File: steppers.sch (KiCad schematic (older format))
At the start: 24 parts, among them J1 HEADER, J10 STEPSTICK, J11 STEPSTICK, J12 STEPSTICK, J2 HEADER, J3 HEADER, J4 STEPSTICK, J5 STEPSTICK, J6 STEPSTICK, J7 HEADER, J8 HEADER, J9 HEADER, P10 CONN_01X04, P11 CONN_01X04, P12 CONN_01X04, P7 CONN_02X04, P8 CONN_01X04, P9 CONN_01X04

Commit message: Added component specifications
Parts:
- C12, C13, C14, C15, C16, C17: Manufacturer (none) -> United Chemi-Con; ManufacturerNo (none) -> EMZR500ADA101MF80G; VoltageRating (none) -> 50V
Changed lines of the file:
@@
 F 2 "capacitors:c_elec_6.3x7.7" H 3800 1425 50  0001 C CNN
 F 3 "" H 3800 1425 50  0000 C CNN
+F 4 "50V" H 3800 1425 135 0001 L CNN "VoltageRating"
+F 5 "EMZR500ADA101MF80G" H 3800 1425 135 0001 L CNN "ManufacturerNo"
+F 6 "United Chemi-Con" H 3800 1425 135 0001 L CNN "Manufacturer"
 	1    3800 1425
 	1    0    0    -1
@@
 F 2 "capacitors:c_elec_6.3x7.7" H 3800 2650 50  0001 C CNN
 F 3 "" H 3800 2650 50  0000 C CNN
+F 4 "50V" H 3800 2650 135 0001 L CNN "VoltageRating"
+F 5 "EMZR500ADA101MF80G" H 3800 2650 135 0001 L CNN "ManufacturerNo"
+F 6 "United Chemi-Con" H 3800 2650 135 0001 L CNN "Manufacturer"
 	1    3800 2650
 	1    0    0    -1
@@
 F 2 "capacitors:c_elec_6.3x7.7" H 3950 3950 50  0001 C CNN
 F 3 "" H 3950 3950 50  0000 C CNN
+F 4 "50V" H 3950 3950 135 0001 L CNN "VoltageRating"
+F 5 "United Chemi-Con" H 3950 3950 135 0001 L CNN "Manufacturer"
+F 6 "EMZR500ADA101MF80G" H 3950 3950 135 0001 L CNN "ManufacturerNo"
 	1    3950 3950
 	1    0    0    -1
@@
 F 2 "capacitors:c_elec_6.3x7.7" H 8900 4075 50  0001 C CNN
 F 3 "" H 8900 4075 50  0000 C CNN
+F 4 "50V" H 8900 4075 135 0001 L CNN "VoltageRating"
+F 5 "EMZR500ADA101MF80G" H 8900 4075 135 0001 L CNN "ManufacturerNo"
+F 6 "United Chemi-Con" H 8900 4075 135 0001 L CNN "Manufacturer"
 	1    8900 4075
 	1    0    0    -1
@@
 F 2 "capacitors:c_elec_6.3x7.7" H 8875 1400 50  0001 C CNN
 F 3 "" H 8875 1400 50  0000 C CNN
+F 4 "50V" H 8875 1400 135 0001 L CNN "VoltageRating"
+F 5 "EMZR500ADA101MF80G" H 8875 1400 135 0001 L CNN "ManufacturerNo"
+F 6 "United Chemi-Con" H 8875 1400 135 0001 L CNN "Manufacturer"
 	1    8875 1400
 	1    0    0    -1
@@
 F 2 "capacitors:c_elec_6.3x7.7" H 8875 2775 50  0001 C CNN
 F 3 "" H 8875 2775 50  0000 C CNN
+F 4 "50V" H 8875 2775 135 0001 L CNN "VoltageRating"
+F 5 "EMZR500ADA101MF80G" H 8875 2775 135 0001 L CNN "ManufacturerNo"
+F 6 "United Chemi-Con" H 8875 2775 135 0001 L CNN "Manufacturer"
 	1    8875 2775
 	1    0    0    -1

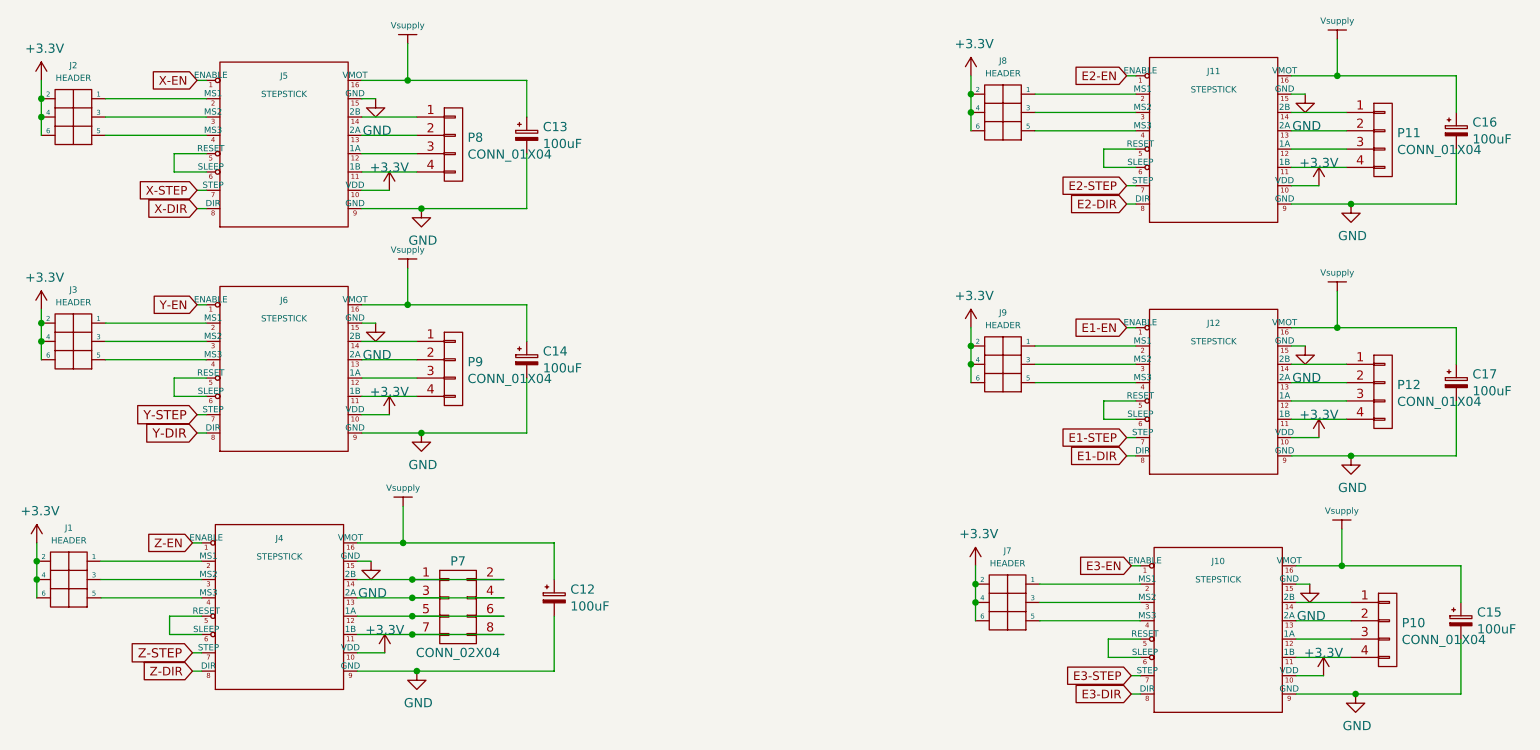
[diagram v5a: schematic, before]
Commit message: Added specifications and manufacturers to component attributes
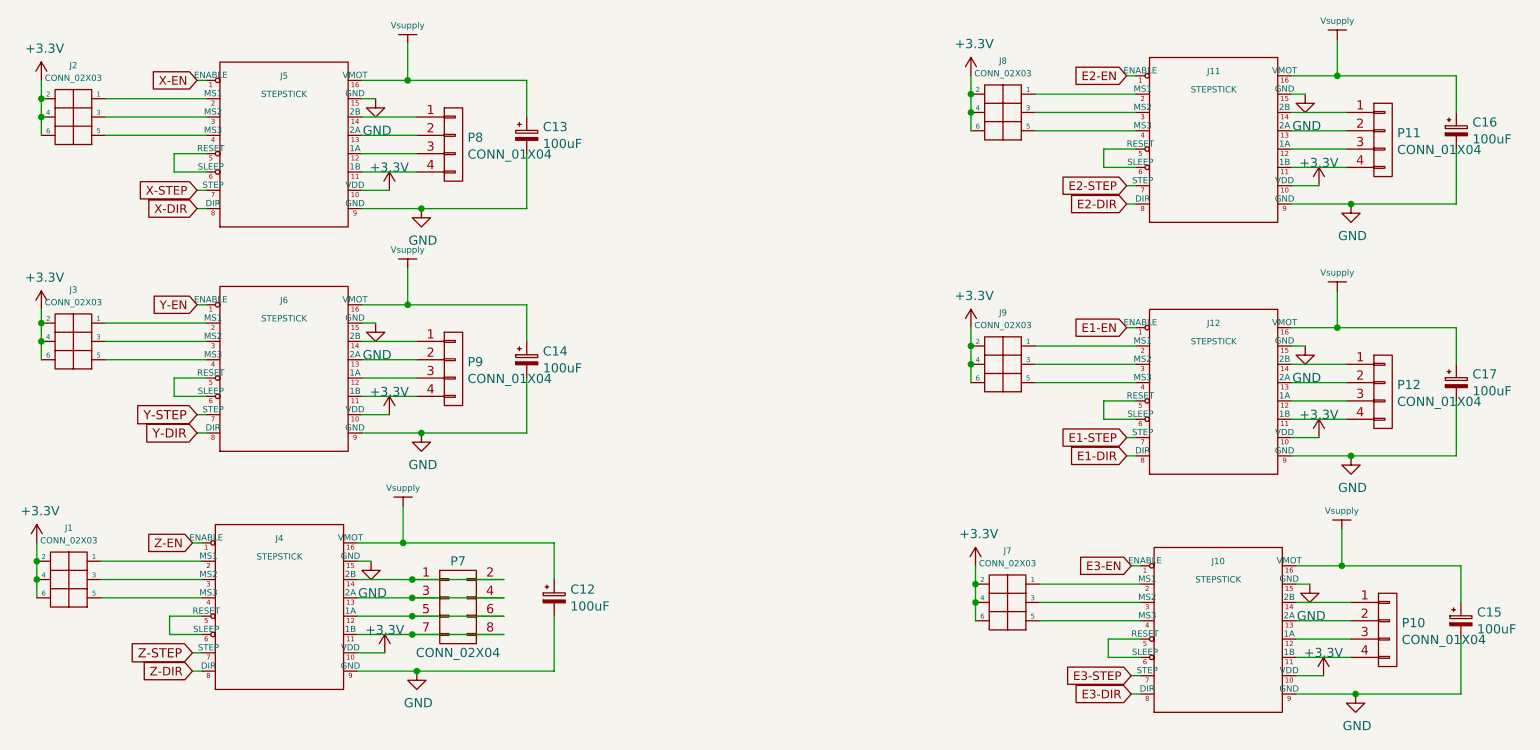
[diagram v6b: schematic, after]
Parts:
- J1, J2, J3, J7, J8, J9: value HEADER -> CONN_02X03; Specification (none) -> 6 pin 2.54mm pitch dual row male header
- J10, J11, J12, J4, J5, J6: Specification (none) -> 2x 8 pin 2.54mm pitch single row female header
- P10, P11, P12, P8, P9: Specification (none) -> 4 pin 2.54mm pitch single row male header
- P7: Specification (none) -> 8 pin 2.54mm pitch dual row male header
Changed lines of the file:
@@
 F 2 "misc:STEPSTICK" H 2025 1925 60  0001 C CNN
 F 3 "" H 2025 1925 60  0000 C CNN
+F 4 "2x 8 pin 2.54mm pitch single row female header" H 2025 1925 135 0001 L CNN "Specification"
 	1    2025 1925
 	1    0    0    -1
@@
 P 1500 1475
 F 0 "J2" H 1675 1907 34  0000 C CNN
-F 1 "HEADER" H 1675 1838 34  0000 C CNN
+F 1 "CONN_02X03" H 1675 1838 34  0000 C CNN
 F 2 "headers:CON_HDR_2x3_2.54mm" H 1500 1475 60  0001 C CNN
 F 3 "" H 1500 1475 60  0000 C CNN
+F 4 "6 pin 2.54mm pitch dual row male header" H 1500 1475 135 0001 L CNN "Specification"
 	1    1500 1475
 	-1   0    0    -1
@@
 F 2 "headers:CON_HDR_1x4_2.54mm" H 3400 1475 50  0001 C CNN
 F 3 "" H 3400 1475 50  0000 C CNN
+F 4 "4 pin 2.54mm pitch single row male header" H 3400 1475 135 0001 L CNN "Specification"
 	1    3400 1475
 	1    0    0    -1
@@
 F 2 "misc:STEPSTICK" H 2025 3150 60  0001 C CNN
 F 3 "" H 2025 3150 60  0000 C CNN
+F 4 "2x 8 pin 2.54mm pitch single row female header" H 2025 3150 135 0001 L CNN "Specification"
 	1    2025 3150
 	1    0    0    -1
@@
 P 1500 2700
 F 0 "J3" H 1675 3132 34  0000 C CNN
-F 1 "HEADER" H 1675 3063 34  0000 C CNN
+F 1 "CONN_02X03" H 1675 3063 34  0000 C CNN
 F 2 "headers:CON_HDR_2x3_2.54mm" H 1500 2700 60  0001 C CNN
 F 3 "" H 1500 2700 60  0000 C CNN
+F 4 "6 pin 2.54mm pitch dual row male header" H 1500 2700 135 0001 L CNN "Specification"
 	1    1500 2700
 	-1   0    0    -1
@@
 F 2 "headers:CON_HDR_1x4_2.54mm" H 3400 2700 50  0001 C CNN
 F 3 "" H 3400 2700 50  0000 C CNN
+F 4 "4 pin 2.54mm pitch single row male header" H 3400 2700 135 0001 L CNN "Specification"
 	1    3400 2700
 	1    0    0    -1
@@
 F 2 "misc:STEPSTICK" H 2000 4450 60  0001 C CNN
 F 3 "" H 2000 4450 60  0000 C CNN
+F 4 "2x 8 pin 2.54mm pitch single row female header" H 2000 4450 135 0001 L CNN "Specification"
 	1    2000 4450
 	1    0    0    -1
@@
 F 2 "misc:STEPSTICK" H 7125 4575 60  0001 C CNN
 F 3 "" H 7125 4575 60  0000 C CNN
+F 4 "2x 8 pin 2.54mm pitch single row female header" H 7125 4575 135 0001 L CNN "Specification"
 	1    7125 4575
 	1    0    0    -1
@@
 P 6600 4125
 F 0 "J7" H 6775 4557 34  0000 C CNN
-F 1 "HEADER" H 6775 4488 34  0000 C CNN
+F 1 "CONN_02X03" H 6775 4488 34  0000 C CNN
 F 2 "headers:CON_HDR_2x3_2.54mm" H 6600 4125 60  0001 C CNN
 F 3 "" H 6600 4125 60  0000 C CNN
+F 4 "6 pin 2.54mm pitch dual row male header" H 6600 4125 135 0001 L CNN "Specification"
 	1    6600 4125
 	-1   0    0    -1
@@
 F 2 "headers:CON_HDR_1x4_2.54mm" H 8500 4125 50  0001 C CNN
 F 3 "" H 8500 4125 50  0000 C CNN
+F 4 "4 pin 2.54mm pitch single row male header" H 8500 4125 135 0001 L CNN "Specification"
 	1    8500 4125
 	1    0    0    -1
@@
 F 2 "misc:STEPSTICK" H 7100 1900 60  0001 C CNN
 F 3 "" H 7100 1900 60  0000 C CNN
+F 4 "2x 8 pin 2.54mm pitch single row female header" H 7100 1900 135 0001 L CNN "Specification"
 	1    7100 1900
 	1    0    0    -1
@@
 P 6575 1450
 F 0 "J8" H 6750 1882 34  0000 C CNN
-F 1 "HEADER" H 6750 1813 34  0000 C CNN
+F 1 "CONN_02X03" H 6750 1813 34  0000 C CNN
 F 2 "headers:CON_HDR_2x3_2.54mm" H 6575 1450 60  0001 C CNN
 F 3 "" H 6575 1450 60  0000 C CNN
+F 4 "6 pin 2.54mm pitch dual row male header" H 6575 1450 135 0001 L CNN "Specification"
 	1    6575 1450
 	-1   0    0    -1
@@
 F 2 "headers:CON_HDR_1x4_2.54mm" H 8475 1450 50  0001 C CNN
 F 3 "" H 8475 1450 50  0000 C CNN
+F 4 "4 pin 2.54mm pitch single row male header" H 8475 1450 135 0001 L CNN "Specification"
 	1    8475 1450
 	1    0    0    -1
@@
 F 2 "misc:STEPSTICK" H 7100 3275 60  0001 C CNN
 F 3 "" H 7100 3275 60  0000 C CNN
+F 4 "2x 8 pin 2.54mm pitch single row female header" H 7100 3275 135 0001 L CNN "Specification"
 	1    7100 3275
 	1    0    0    -1
@@
 P 6575 2825
 F 0 "J9" H 6750 3257 34  0000 C CNN
-F 1 "HEADER" H 6750 3188 34  0000 C CNN
+F 1 "CONN_02X03" H 6750 3188 34  0000 C CNN
 F 2 "headers:CON_HDR_2x3_2.54mm" H 6575 2825 60  0001 C CNN
 F 3 "" H 6575 2825 60  0000 C CNN
+F 4 "6 pin 2.54mm pitch dual row male header" H 6575 2825 135 0001 L CNN "Specification"
 	1    6575 2825
 	-1   0    0    -1
@@
 F 2 "headers:CON_HDR_1x4_2.54mm" H 8475 2825 50  0001 C CNN
 F 3 "" H 8475 2825 50  0000 C CNN
+F 4 "4 pin 2.54mm pitch single row male header" H 8475 2825 135 0001 L CNN "Specification"
 	1    8475 2825
 	1    0    0    -1
@@
 F 2 "headers:CON_HDR_2x4_2.54mm" H 3425 2800 50  0001 C CNN
 F 3 "" H 3425 2800 50  0000 C CNN
+F 4 "8 pin 2.54mm pitch dual row male header" H 3425 4000 135 0001 L CNN "Specification"
 	1    3425 4000
 	1    0    0    -1
@@
 P 1475 4000
 F 0 "J1" H 1650 4432 34  0000 C CNN
-F 1 "HEADER" H 1650 4363 34  0000 C CNN
+F 1 "CONN_02X03" H 1650 4363 34  0000 C CNN
 F 2 "headers:CON_HDR_2x3_2.54mm" H 1475 4000 60  0001 C CNN
 F 3 "" H 1475 4000 60  0000 C CNN
+F 4 "6 pin 2.54mm pitch dual row male header" H 1475 4000 135 0001 L CNN "Specification"
 	1    1475 4000
 	-1   0    0    -1
